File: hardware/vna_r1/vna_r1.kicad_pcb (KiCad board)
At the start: 4 copper layers, 193.6 x 146.5 mm, 440 parts, among them IC1301 SN74LVC1G07DCK, IC1302 TPD4S012DRYR, IC1303 TPD4S012DRYR, J1001 Conn_02x10_Odd_Even, J1002 Conn_02x10_Odd_Even, J1003 Conn_02x05_Odd_Even, J1201 DB15_FEMALE_MountingHoles, J1202 BARREL_JACK, J1301 0480254000, J1302 USB_A, J901 CONN_01X02, Q1201 Q_PMOS_DGS, Q1301 24 MHz, Q1302 24 MHz, U1001 CONN_SMA_2GND, U1002 CONN_SMA_2GND, U1003 CONN_SMA_2GND, U1004 CONN_SMA_2GND, U1005 CONN_SMA_2GND, U1006 CONN_SMA_2GND, U1007 CONN_SMA_2GND, U1008 CONN_SMA_2GND, U1101 AD9577, U1102 NB3N551, U1201 CONN_SMA, U1202 CONN_SMA, U1301 OSD3358-512M-BSM, U1302 74HC244, U1303 LAN8710A, U1304 TPS2051, U1305 MICROSD, U502 ad9864, U602 ad9864, U702 ad9864, U802 ad9864, U902 ADP7158, U903 ADP7158, U904 OKR-T/3-W12-C, X1301 10118192-0001LF, Y1101 26 MHz 7M-26.000MEEQ-T

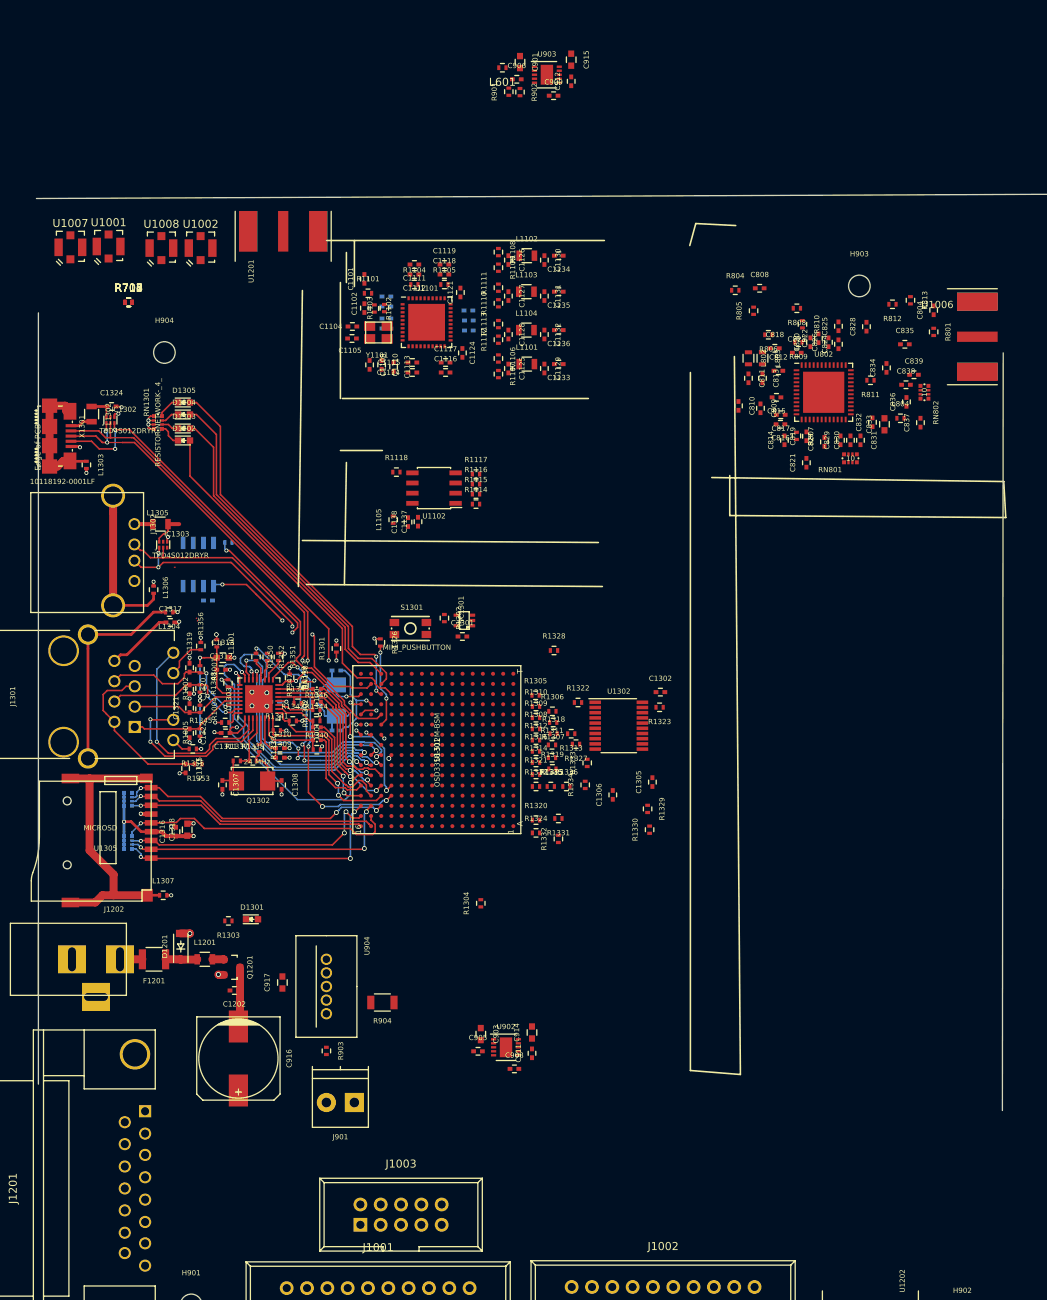
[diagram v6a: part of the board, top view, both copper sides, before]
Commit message: footprint assignment for vna r1 synth and demod
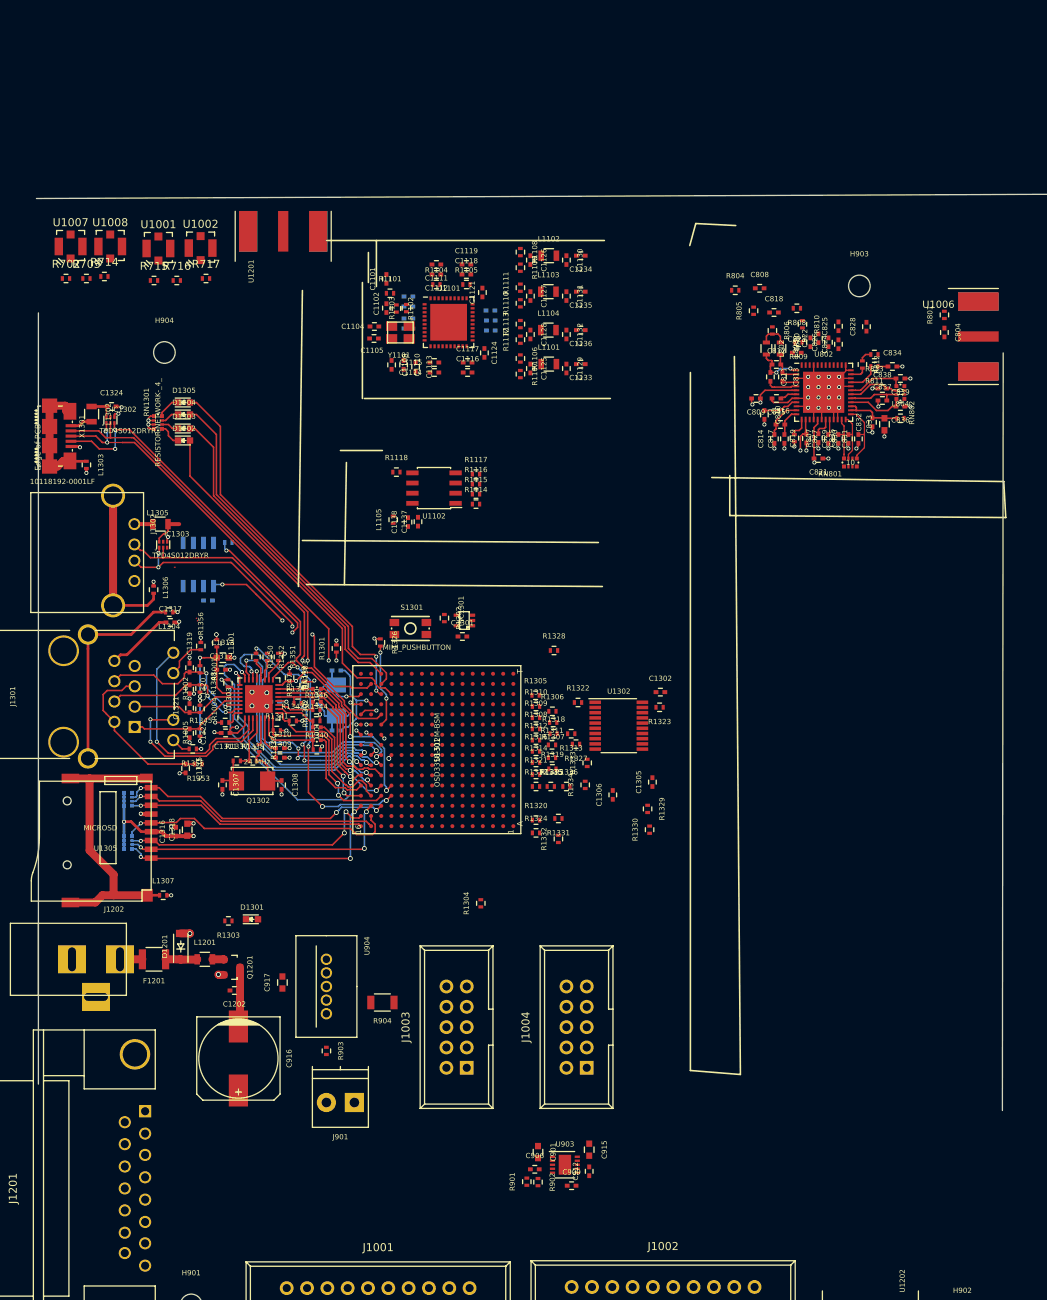
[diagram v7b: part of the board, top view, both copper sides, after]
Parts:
- removed C903, C914: 10 uF, Capacitors_SMD:C_0603
- removed C905, C908, C911: 1 uF, Capacitors_SMD:C_0402
- removed L601: L_Small, Resistors_SMD:R_0402
- removed U902: ADP7158, Housings_DFN_QFN:DFN-10-1EP_3x3mm_Pitch0.5mm
- added J1004: Conn_02x05_Odd_Even, Connect:IDC_Header_Straight_10pins, F.Cu at (362.5, -101.8)
- moved C901 136.3 mm to (356.4, -91.3)
- moved C906 136.3 mm to (356.1, -89.2)
- moved C909 136.3 mm to (360.6, -87.1)
- moved C912 136.3 mm to (362.9, -88.9)
- moved C915 136.3 mm to (362.9, -91.6)
- moved R901 136.3 mm to (355.1, -87.6)
- moved R902 136.3 mm to (356.4, -87.5)
- moved U903 136.3 mm to (359.8, -89.7)
- moved J1003 23.7 mm to (347.5, -101.8), turned to 90 degrees
- moved C835 15.9 mm to (391.5, -180.6), turned to 270 degrees
- moved R717 10.1 mm to (314.9, -200.5)
- moved R812 8.41 mm to (397.0, -189.8), turned to 270 degrees
- moved R702 8.37 mm to (297.4, -200.5)
- moved R813 8.14 mm to (398.5, -191.0), turned to 180 degrees
- moved R716 6.61 mm to (311.3, -200.2)
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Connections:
- C1103 pad 1: VDD_RTC -> +3V3
- C1106 pad 1: VDD_RTC -> +3V3
- C1107 pad 1: VDD_RTC -> +3V3
- C1108 pad 1: VDD_RTC -> +3V3
- C1109 pad 1: VDD_RTC -> +3V3
- C1110 pad 1: VDD_RTC -> +3V3
- C1111 pad 1: VDD_RTC -> +3V3
- C1112 pad 1: VDD_RTC -> +3V3
- C1114 pad 1: VDD_RTC -> +3V3
- C1115 pad 1: VDD_RTC -> +3V3
- C1116 pad 1: VDD_RTC -> +3V3
- C1117 pad 1: VDD_RTC -> +3V3
- C1118 pad 1: VDD_RTC -> +3V3
- C1119 pad 1: VDD_RTC -> +3V3
- C1120 pad 1: VDD_RTC -> +3V3
- C1121 pad 1: VDD_RTC -> +3V3
- C1122 pad 1: VDD_RTC -> +3V3
- C1123 pad 1: VDD_RTC -> +3V3
- C1124 pad 1: VDD_RTC -> +3V3
- C509 pad 1: USB_DC -> +3V3
- C510 pad 1: USB_DC -> +3V3
- C518 pad 2: USB_DC -> +3V3
- C519 pad 2: USB_DC -> +3V3
- C521 pad 2: USB_DC -> +3V3
- C525 pad 2: USB_DC -> +3V3
- C528 pad 2: USB_DC -> +3V3
- C609 pad 1: USB_DC -> +3V3
- C610 pad 1: USB_DC -> +3V3
- C618 pad 2: USB_DC -> +3V3
- C619 pad 2: USB_DC -> +3V3
- C621 pad 2: USB_DC -> +3V3
- C625 pad 2: USB_DC -> +3V3
- C628 pad 2: USB_DC -> +3V3
- C709 pad 1: USB_DC -> +3V3
- C710 pad 1: USB_DC -> +3V3
- C718 pad 2: USB_DC -> +3V3
- C719 pad 2: USB_DC -> +3V3
- C721 pad 2: USB_DC -> +3V3
- C725 pad 2: USB_DC -> +3V3
- C728 pad 2: USB_DC -> +3V3
- C809 pad 1: USB_DC -> +3V3
- C810 pad 1: USB_DC -> +3V3
- C818 pad 2: USB_DC -> +3V3
- C819 pad 2: USB_DC -> +3V3
- C821 pad 2: USB_DC -> +3V3
- C825 pad 2: USB_DC -> +3V3
- C828 pad 2: USB_DC -> +3V3
- C901 pad 2: VDD_RTC -> +3V3
- L1105 pad 1: VDD_RTC -> +3V3
- L504 pad 2: USB_DC -> +3V3
- L604 pad 2: USB_DC -> +3V3
- L704 pad 2: USB_DC -> +3V3
- L804 pad 2: USB_DC -> +3V3
- R1102 pad 1: VDD_RTC -> +3V3
- R1104 pad 1: VDD_RTC -> +3V3
- R1105 pad 1: VDD_RTC -> +3V3
- R1106 pad 1: VDD_RTC -> +3V3
- R1108 pad 1: VDD_RTC -> +3V3
- R1110 pad 1: VDD_RTC -> +3V3
- R1112 pad 1: VDD_RTC -> +3V3
- R506 pad 1: USB_DC -> +3V3
- R606 pad 1: USB_DC -> +3V3
- R706 pad 1: USB_DC -> +3V3
- R806 pad 1: USB_DC -> +3V3
- U1101 pad 1: VDD_RTC -> +3V3
- U1101 pad 10: VDD_RTC -> +3V3
- U1101 pad 14: VDD_RTC -> +3V3
- U1101 pad 19: VDD_RTC -> +3V3
- U1101 pad 2: VDD_RTC -> +3V3
- U1101 pad 21: VDD_RTC -> +3V3
- U1101 pad 24: VDD_RTC -> +3V3
- U1101 pad 25: VDD_RTC -> +3V3
- U1101 pad 27: VDD_RTC -> +3V3
- U1101 pad 30: VDD_RTC -> +3V3
- U1101 pad 32: VDD_RTC -> +3V3
- U1101 pad 38: VDD_RTC -> +3V3
- U1101 pad 4: VDD_RTC -> +3V3
- U1101 pad 5: VDD_RTC -> +3V3
- U1301 pad C13: /3V3_DEMOD_EN -> (no net)
- U502 pad 14: USB_DC -> +3V3
- U502 pad 17: USB_DC -> +3V3
- U502 pad 39: USB_DC -> +3V3
- U502 pad 40: USB_DC -> +3V3
- U502 pad 48: USB_DC -> +3V3
- U502 pad 6: USB_DC -> +3V3
- U502 pad 9: USB_DC -> +3V3
- U602 pad 14: USB_DC -> +3V3
- U602 pad 17: USB_DC -> +3V3
- U602 pad 39: USB_DC -> +3V3
- U602 pad 40: USB_DC -> +3V3
- U602 pad 48: USB_DC -> +3V3
- U602 pad 6: USB_DC -> +3V3
- U602 pad 9: USB_DC -> +3V3
- U702 pad 14: USB_DC -> +3V3
- U702 pad 17: USB_DC -> +3V3
- U702 pad 39: USB_DC -> +3V3
- U702 pad 40: USB_DC -> +3V3
- U702 pad 48: USB_DC -> +3V3
- U702 pad 6: USB_DC -> +3V3
- U702 pad 9: USB_DC -> +3V3
- U802 pad 14: USB_DC -> +3V3
- U802 pad 17: USB_DC -> +3V3
- U802 pad 39: USB_DC -> +3V3
- U802 pad 40: USB_DC -> +3V3
- U802 pad 48: USB_DC -> +3V3
- U802 pad 6: USB_DC -> +3V3
- U802 pad 9: USB_DC -> +3V3
- U903 pad 1: VDD_RTC -> +3V3
- U903 pad 2: VDD_RTC -> +3V3
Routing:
- net GND: track 31.0 -> 71.3 mm, vias 43 -> 77
- net +3V3: track 0.00 -> 20.2 mm, vias 0 -> 3
- net Net-(C831-Pad2): track 0.00 -> 7.76 mm
- net Net-(C832-Pad2): track 0.00 -> 7.69 mm
- net Net-(C836-Pad2): track 0.00 -> 7.25 mm
- net Net-(C839-Pad2): track 0.00 -> 7.22 mm
- net Net-(C837-Pad2): track 0.00 -> 6.81 mm
- net Net-(C838-Pad2): track 0.00 -> 6.55 mm
- net Net-(C811-Pad1): track 0.00 -> 6.41 mm, vias 0 -> 2
- net Net-(C830-Pad2): track 0.00 -> 6.10 mm
- net Net-(C829-Pad2): track 0.00 -> 5.71 mm
- net Net-(C814-Pad2): track 0.00 -> 4.89 mm
- net Net-(C812-Pad2): track 0.00 -> 4.20 mm
- net Net-(C811-Pad2): track 0.00 -> 3.89 mm
- net Net-(R811-Pad2): track 0.00 -> 3.87 mm
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
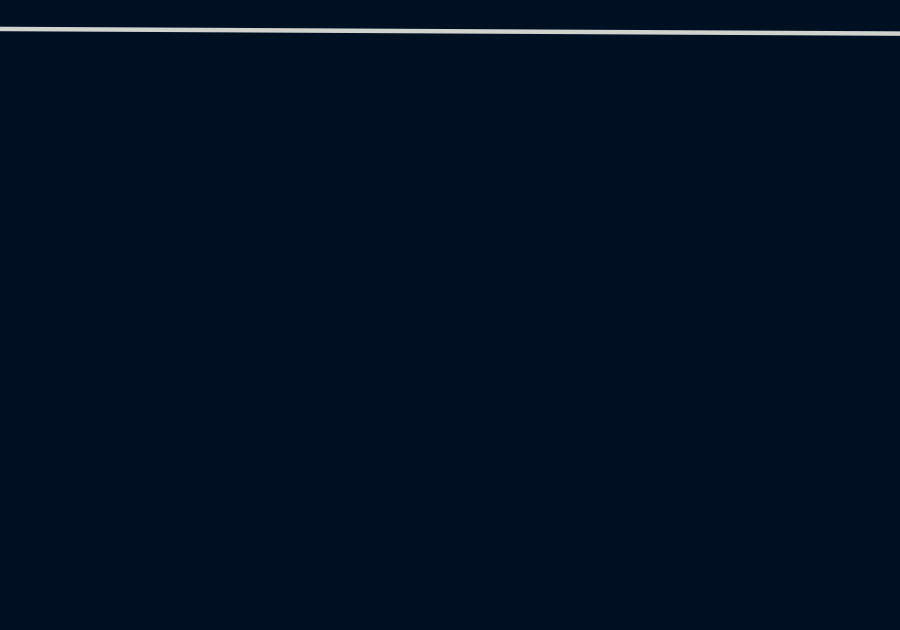
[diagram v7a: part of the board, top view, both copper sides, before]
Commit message: component placement on vna r1 demod
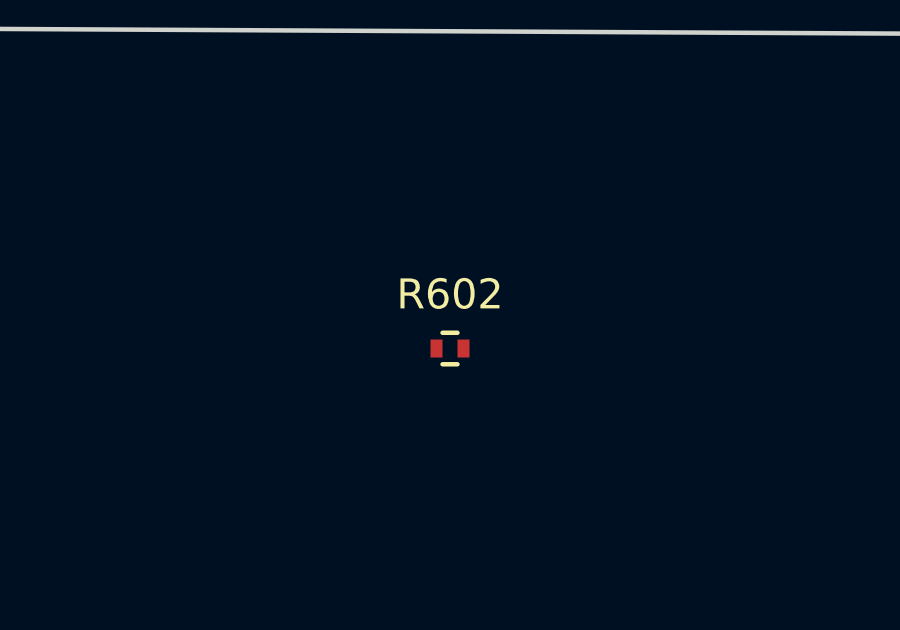
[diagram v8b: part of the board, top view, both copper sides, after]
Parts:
- added R602: R_Small, Resistors_SMD:R_0402, F.Cu at (390.4, -54.7)
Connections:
- J1001 pad 12: (no net) -> /LO_3V3_EN
- J1001 pad 13: (no net) -> /LO_-5V_EN
- J1001 pad 6: (no net) -> /LO_PORT_SEL
- J1001 pad 7: (no net) -> /LO_DAC_CS
- R1333 pad 1: VDD_RTC -> +3V3
- U1102 pad 8: /3V3_PLL_SENSE -> /ADC_CLK_EN
- U1301 pad A4: (no net) -> /LO_AMP_EN
- U1301 pad A8: /control/VDD_RF_MON -> (no net)
- U1301 pad B8: /control/VDD_LO_MON -> (no net)
- U1301 pad C13: (no net) -> /ADC_CLK_EN
- U1301 pad C5: (no net) -> /3V3_DEMOD_EXT_EN
- U1301 pad F3: /3V3_DEMOD_EXT_EN -> (no net)
- U1301 pad N14: (no net) -> /LO_3V3_EN
- U1301 pad P15: (no net) -> /LO_PORT_SEL
- U1301 pad R16: (no net) -> /LO_DAC_CS
- U1301 pad R3: (no net) -> /LO_-5V_EN
- U903 pad 3: /3V3_PLL_SENSE -> Net-(R602-Pad1)
